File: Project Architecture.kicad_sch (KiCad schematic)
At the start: 0 parts

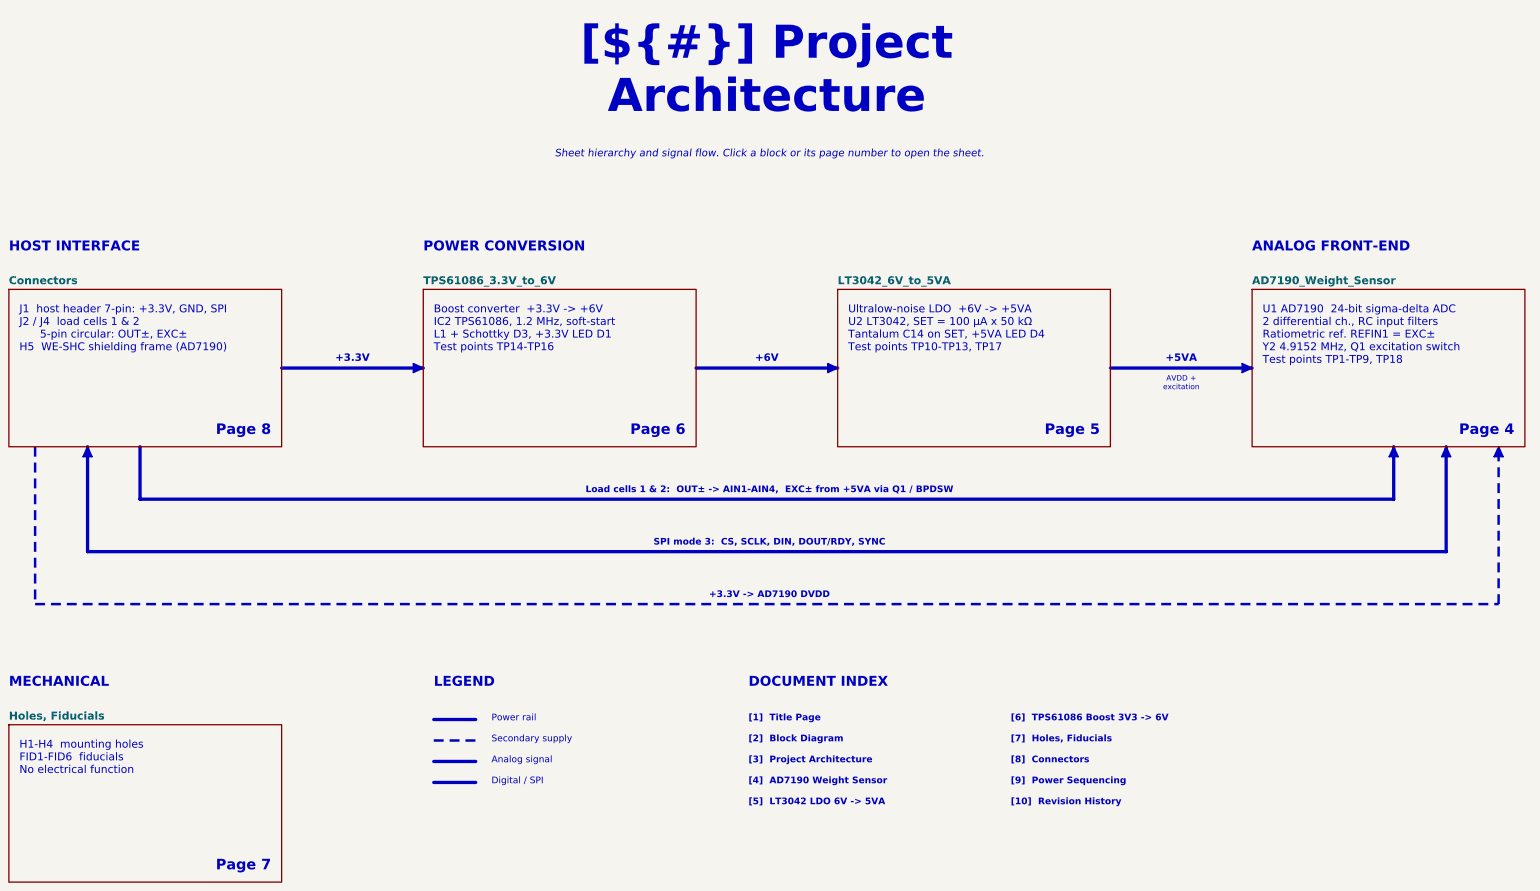
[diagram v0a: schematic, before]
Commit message: Restyle the schematic like OPEN_PHASE, merge the power sheets, rework the bottom silkscreen
- Schematic: all sheets on A3 in the OPEN_PHASE look (red header bands,
  DESCRIPTION / DESIGN NOTE / LAYOUT NOTE / CALCULS & BUDGET panels in
  French, TEST POINTS panel, References in the title block)
- Title block: INGENIERIE FRANCE logo in KDT_Template_GIT.kicad_wks,
  per-sheet logo images removed
- Power - Sequencing rebuilt with curves from LTspice simulations 01-04
- TPS61086 and LT3042 sheets merged into Power Supply - Analog Rails
  (page 5, keeps the TPS sheet UUID); pages renumbered to 9, local nets
  renamed to /Project Architecture/Power_Supply/*, PCB links updated
- PCB: per-rail net colours (+3.3V, +6V, +5VA, GND) as on OPEN_PHASE
- PCB B.SilkS: test point pills with Arial Black knockout names, J1
  pinout cells, E+/E-/S+/S- tags on the M12 pads, CELL 1 / CELL 2 titles
  and a LOAD CELL wiring panel

Netlist connectivity, ERC (2 warnings) and copper DRC unchanged;
schematic parity clean.

Co-Authored-By: Claude Opus 5.5 <noreply@anthropic.com>
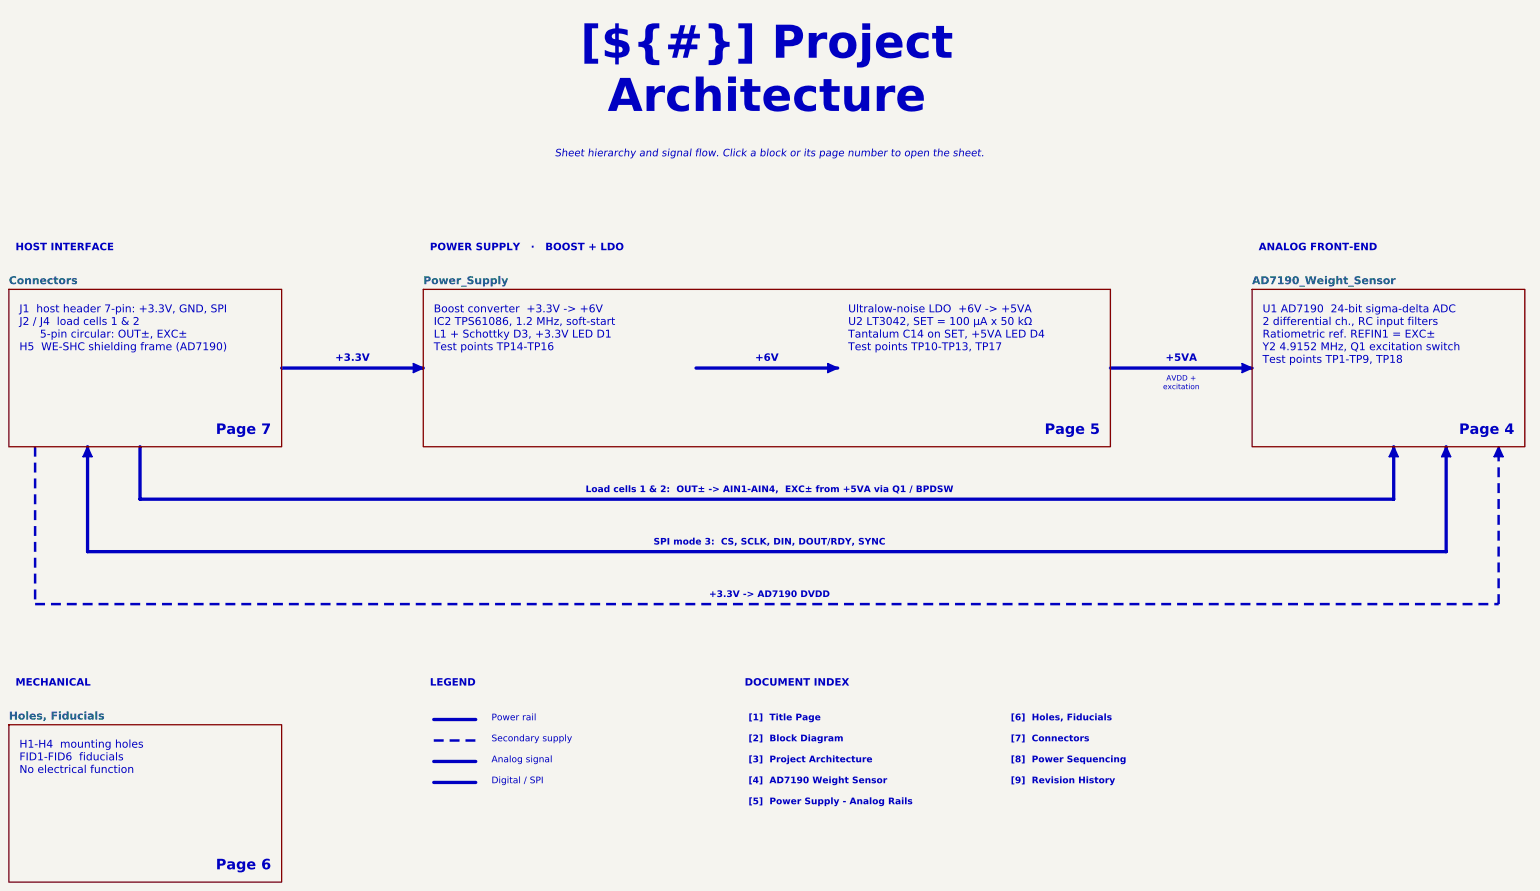
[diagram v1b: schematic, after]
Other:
- sheet TPS61086_3.3V_to_6V renamed Power_Supply
- removed sheet LT3042_6V_to_5VA
- sheet Power_Supply: file TPS61086 - Boost 3V3 to 6V.kicad_sch -> Power Supply - Analog Rails.kicad_sch
- note added: "[5] Power Supply - Analog Rails"
- note added: "[6] Holes, Fiducials"
- note added: "[7] Connectors"
- note added: "[8] Power Sequencing"
- note added: "[9] Revision History"
- note removed: "ANALOG FRONT-END"
- note removed: "DOCUMENT INDEX"
- note removed: "HOST INTERFACE"
- note removed: "LEGEND"
- note removed: "MECHANICAL"
- note removed: "POWER CONVERSION"
- note removed: "Page 8"
- note removed: "[10] Revision History"
- note removed: "[5] LT3042 LDO 6V -> 5VA"
- note removed: "[6] TPS61086 Boost 3V3 -> 6V"
- note removed: "[7] Holes, Fiducials"
- note removed: "[8] Connectors"
- note removed: "[9] Power Sequencing"
